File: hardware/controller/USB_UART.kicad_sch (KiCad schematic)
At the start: 0 parts

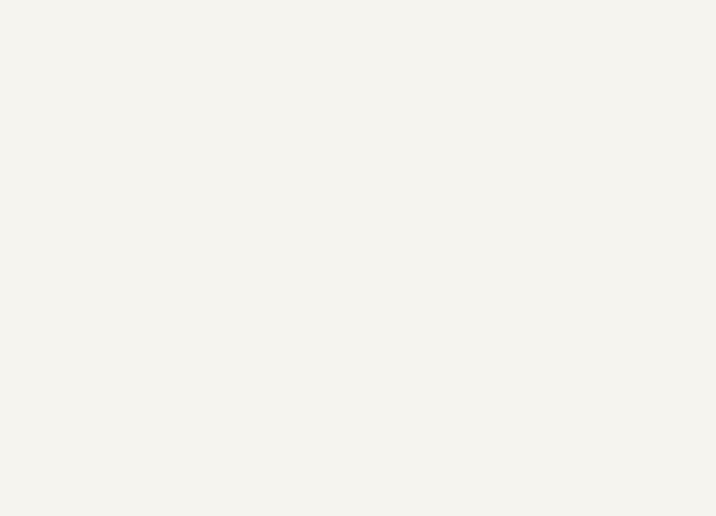
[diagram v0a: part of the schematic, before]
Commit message: added LED IC's and USB UART bridge
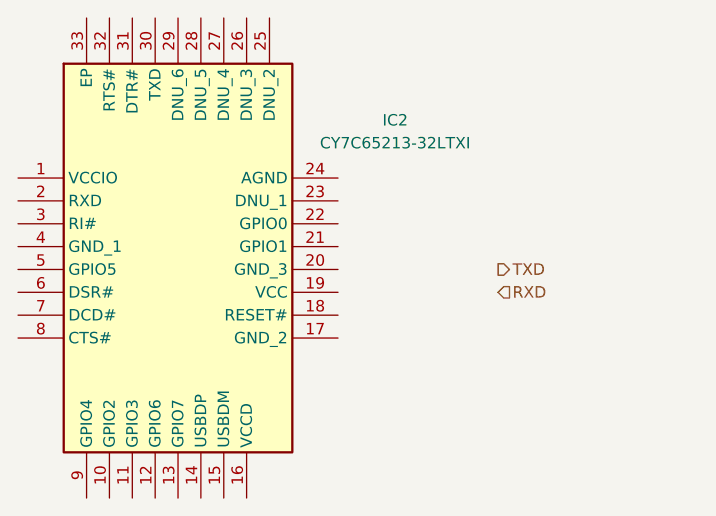
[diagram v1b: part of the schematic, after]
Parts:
- added IC2: CY7C65213-32LTXI, QFN50P500X500X100-33N-D, symbol SamacSys_Parts:CY7C65213-32LTXI
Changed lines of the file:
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@@
+		)
+	)
+	(hierarchical_label "RXD"
+		(shape input)
+		(at 148.59 83.82 0)
+		(effects
+			(font
+				(size 1.27 1.27)
+			)
+			(justify left)
 		)
 	)
@@
 		)
 	)
+	(hierarchical_label "TXD"
+		(shape output)
+		(at 148.59 81.28 0)
+		(effects
+			(font
+				(size 1.27 1.27)
+			)
+			(justify left)
+		)
+	)
+	(symbol
+		(lib_id "SamacSys_Parts:CY7C65213-32LTXI")
+		(at 95.25 71.12 0)
+		(unit 1)
+		(exclude_from_sim no)
+		(in_bom yes)
+		(on_board yes)
+		(dnp no)
+		(fields_autoplaced yes)
+		(property "Reference" "IC2"
+			(at 137.16 64.6998 0)
+			(effects
+				(font
+					(size 1.27 1.27)
+				)
+			)
+		)
+		(property "Value" "CY7C65213-32LTXI"
+			(at 137.16 67.2398 0)
+			(effects
+				(font
+					(size 1.27 1.27)
+				)
+			)
+		)
+		(property "Footprint" "QFN50P500X500X100-33N-D"
+			(at 127 155.88 0)
+			(effects
+				(font
+					(size 1.27 1.27)
+				)
+				(justify left top)
+				(hide yes)
+			)
+		)
+		(property "Datasheet" "https://www.cypress.com/file/139881/download"
+			(at 127 255.88 0)
+			(effects
+				(font
+					(size 1.27 1.27)
+				)
+				(justify left top)
+				(hide yes)
+			)
+		)
+		(property "Description" "USB Interface IC USB-UART LP Bridge Controller"
+			(at 95.25 71.12 0)
+			(effects
+				(font
+					(size 1.27 1.27)
+				)
+				(hide yes)
+			)
+		)
+		(property "Height" "1"
+			(at 127 455.88 0)
+			(effects
+				(font
+					(size 1.27 1.27)
+				)
+				(justify left top)
+				(hide yes)
+			)
+		)
+		(property "Mouser Part Number" "727-CY7C65213-32LTXI"
+			(at 127 555.88 0)
+			(effects
+				(font
+					(size 1.27 1.27)
+				)
+				(justify left top)
+				(hide yes)
+			)
+		)
+		(property "Mouser Price/Stock" "https://www.mouser.co.uk/ProductDetail/Cypress-Semiconductor/CY7C65213-32LTXI?qs=zaNmQhktveH29yVGSodaDg%3D%3D"
+			(at 127 655.88 0)
+			(effects
+				(font
+					(size 1.27 1.27)
+				)
+				(justify left top)
+				(hide yes)
+			)
+		)
+		(property "Manufacturer_Name" "Infineon"
+			(at 127 755.88 0)
+			(effects
+				(font
+					(size 1.27 1.27)
+				)
+				(justify left top)
+				(hide yes)
+			)
+		)
+		(property "Manufacturer_Part_Number" "CY7C65213-32LTXI"
+			(at 127 855.88 0)
+			(effects
+				(font
+					(size 1.27 1.27)
+				)
+				(justify left top)
+				(hide yes)
+			)
+		)
+		(pin "8"
+		)
+		(pin "3"
+		)
+		(pin "13"
+		)
+		(pin "25"
+		)
+		(pin "16"
+		)
+		(pin "6"
+		)
+		(pin "21"
+		)
+		(pin "19"
+		)
+		(pin "33"
+		)
+		(pin "5"
+		)
+		(pin "2"
+		)
+		(pin "9"
+		)
+		(pin "11"
+		)
+		(pin "30"
+		)
+		(pin "31"
+		)
+		(pin "12"
+		)
+		(pin "28"
+		)
+		(pin "27"
+		)
+		(pin "32"
+		)
+		(pin "4"
+		)
+		(pin "7"
+		)
+		(pin "29"
+		)
+		(pin "15"
+		)
+		(pin "1"
+		)
+		(pin "14"
+		)
+		(pin "10"
+		)
+		(pin "26"
+		)
+		(pin "24"
+		)
+		(pin "23"
+		)
+		(pin "22"
+		)
+		(pin "20"
+		)
+		(pin "17"
+		)
+		(pin "18"
+		)
+		(instances
+			(project ""
+				(path "/869bea87-c885-4ead-826b-3f34ceacafad/6716075d-3941-4cbb-90c0-6bb554220bff"
+					(reference "IC2")
+					(unit 1)
+				)
+			)
+		)
+	)

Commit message: asdasd
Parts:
- renumbered IC2 to IC1
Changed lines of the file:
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@@
 		(dnp no)
 		(fields_autoplaced yes)
-		(property "Reference" "IC2"
+		(property "Reference" "IC1"
 			(at 137.16 64.6998 0)
 			(effects
@@
 			(project ""
 				(path "/869bea87-c885-4ead-826b-3f34ceacafad/6716075d-3941-4cbb-90c0-6bb554220bff"
-					(reference "IC2")
+					(reference "IC1")
 					(unit 1)
 				)

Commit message: a
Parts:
- removed IC1: CY7C65213-32LTXI, QFN50P500X500X100-33N-D, symbol SamacSys_Parts:CY7C65213-32LTXI
- added C13: 4u3, symbol Device:C
- added C14: u1, symbol Device:C
- added IC3: CP2102N-A02-GQFN28, QFN50P500X500X80-29N-D, symbol SamacSys_Parts:CP2102N-A02-GQFN28
- added R27: 22k5, symbol Device:R
- added R28: 47k5, symbol Device:R
- added R29: 2k, symbol Device:R
- added R30: 10k, symbol Device:R
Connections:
- net RXD: now also IC3.25 (RXD)
- net TXD: now also IC3.26 (TXD)
- new net: IC3.11 (SUSPENDB), R30.2
- new net: IC3.8 (VBUS), R27.2, R28.2
- new net: IC3.9 (RSTB), R29.1
- new net +3V3: C13.1, C14.1, IC3.6 (VDD), IC3.7 (VREGIN), R29.2
- new net DTR: IC3.28 (DTR)
- new net GND: C13.2, C14.2, IC3.29 (BGND), IC3.3 (GND), R28.1, R30.1
- new net RTS: IC3.24 (RTS)
- new net USB+: IC3.4 (D+)
- new net USB-: IC3.5 (D-)
- new net VBUS: R27.1
- no-connect marks 0 -> 15

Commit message: fixed bus stuff
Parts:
- renumbered C13 to C12, C14 to C13, IC3 to IC1, R29 to R11, R27 to R12, R28 to R13, R30 to R14
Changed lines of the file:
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@@
 		(on_board yes)
 		(dnp no)
-		(property "Reference" "R30"
+		(property "Reference" "R14"
 			(at 118.11 130.81 0)
 			(effects
@@
 			(project "controller"
 				(path "/869bea87-c885-4ead-826b-3f34ceacafad/6716075d-3941-4cbb-90c0-6bb554220bff"
-					(reference "R30")
+					(reference "R14")
 					(unit 1)
 				)
@@
 		(on_board yes)
 		(dnp no)
-		(property "Reference" "IC3"
+		(property "Reference" "IC1"
 			(at 125.984 65.786 0)
 			(effects
@@
 			(project ""
 				(path "/869bea87-c885-4ead-826b-3f34ceacafad/6716075d-3941-4cbb-90c0-6bb554220bff"
-					(reference "IC3")
+					(reference "IC1")
 					(unit 1)
 				)
@@
 		(dnp no)
 		(fields_autoplaced yes)
-		(property "Reference" "C14"
+		(property "Reference" "C13"
 			(at 96.52 107.9499 0)
 			(effects
@@
 			(project "controller"
 				(path "/869bea87-c885-4ead-826b-3f34ceacafad/6716075d-3941-4cbb-90c0-6bb554220bff"
-					(reference "C14")
+					(reference "C13")
 					(unit 1)
 				)
@@
 		(on_board yes)
 		(dnp no)
-		(property "Reference" "#PWR045"
+		(property "Reference" "#PWR035"
 			(at 86.36 107.95 0)
 			(effects
@@
 			(project ""
 				(path "/869bea87-c885-4ead-826b-3f34ceacafad/6716075d-3941-4cbb-90c0-6bb554220bff"
-					(reference "#PWR045")
+					(reference "#PWR035")
 					(unit 1)
 				)
@@
 		(on_board yes)
 		(dnp no)
-		(property "Reference" "R27"
+		(property "Reference" "R12"
 			(at 93.98 122.428 90)
 			(effects
@@
 			(project ""
 				(path "/869bea87-c885-4ead-826b-3f34ceacafad/6716075d-3941-4cbb-90c0-6bb554220bff"
-					(reference "R27")
+					(reference "R12")
 					(unit 1)
 				)
@@
 		(dnp no)
 		(fields_autoplaced yes)
-		(property "Reference" "#PWR048"
+		(property "Reference" "#PWR038"
 			(at 124.46 142.24 0)
 			(effects
@@
 			(project "controller"
 				(path "/869bea87-c885-4ead-826b-3f34ceacafad/6716075d-3941-4cbb-90c0-6bb554220bff"
-					(reference "#PWR048")
+					(reference "#PWR038")
 					(unit 1)
 				)
@@
 		(dnp no)
 		(fields_autoplaced yes)
-		(property "Reference" "#PWR046"
+		(property "Reference" "#PWR036"
 			(at 87.63 121.92 0)
 			(effects
@@
 			(project ""
 				(path "/869bea87-c885-4ead-826b-3f34ceacafad/6716075d-3941-4cbb-90c0-6bb554220bff"
-					(reference "#PWR046")
+					(reference "#PWR036")
 					(unit 1)
 				)
@@
 		(dnp no)
 		(fields_autoplaced yes)
-		(property "Reference" "R28"
+		(property "Reference" "R13"
 			(at 101.6 130.8099 0)
 			(effects
@@
 			(project "controller"
 				(path "/869bea87-c885-4ead-826b-3f34ceacafad/6716075d-3941-4cbb-90c0-6bb554220bff"
-					(reference "R28")
+					(reference "R13")
 					(unit 1)
 				)
@@
 		(on_board yes)
 		(dnp no)
-		(property "Reference" "#PWR036"
+		(property "Reference" "#PWR034"
 			(at 85.09 85.09 0)
 			(effects
@@
 			(project "controller"
 				(path "/869bea87-c885-4ead-826b-3f34ceacafad/6716075d-3941-4cbb-90c0-6bb554220bff"
-					(reference "#PWR036")
+					(reference "#PWR034")
 					(unit 1)
 				)
@@
 		(dnp no)
 		(fields_autoplaced yes)
-		(property "Reference" "C13"
+		(property "Reference" "C12"
 			(at 85.09 107.9499 0)
 			(effects
@@
 			(project ""
 				(path "/869bea87-c885-4ead-826b-3f34ceacafad/6716075d-3941-4cbb-90c0-6bb554220bff"
-					(reference "C13")
+					(reference "C12")
 					(unit 1)
 				)
@@
 		(dnp no)
 		(fields_autoplaced yes)
-		(property "Reference" "#PWR037"
+		(property "Reference" "#PWR039"
 			(at 133.35 142.24 0)
 			(effects
@@
 			(project "controller"
 				(path "/869bea87-c885-4ead-826b-3f34ceacafad/6716075d-3941-4cbb-90c0-6bb554220bff"
-					(reference "#PWR037")
+					(reference "#PWR039")
 					(unit 1)
 				)
@@
 		(on_board yes)
 		(dnp no)
-		(property "Reference" "R29"
+		(property "Reference" "R11"
 			(at 86.36 83.82 0)
 			(effects
@@
 			(project "controller"
 				(path "/869bea87-c885-4ead-826b-3f34ceacafad/6716075d-3941-4cbb-90c0-6bb554220bff"
-					(reference "R29")
+					(reference "R11")
 					(unit 1)
 				)
@@
 		(dnp no)
 		(fields_autoplaced yes)
-		(property "Reference" "#PWR047"
+		(property "Reference" "#PWR037"
 			(at 99.06 142.24 0)
 			(effects
@@
 			(project "controller"
 				(path "/869bea87-c885-4ead-826b-3f34ceacafad/6716075d-3941-4cbb-90c0-6bb554220bff"
-					(reference "#PWR047")
-					(unit 1)
-				)
+					(reference "#PWR037")
+					(unit 1)
+				)

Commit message: modified power circuitry
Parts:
- IC1: footprint QFN50P500X500X80-29N-D -> SamacSys_Parts:QFN50P500X500X80-29N-D
- R11: value 2k -> 1k
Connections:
- net DTR renamed UART.DTR
- net RTS renamed UART.RTS
- net RXD renamed UART.RXD
- net TXD renamed UART.TXD
- net VBUS renamed USBC_VBUS

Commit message: finished first rev of controller schematic minus actually finding passive components. moved some features to rev2 todo
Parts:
- R12: value 22k5 -> 22k1
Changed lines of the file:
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@@
 			)
 		)
-		(property "Value" "22k5"
+		(property "Value" "22k1"
 			(at 93.98 124.968 90)
 			(effects

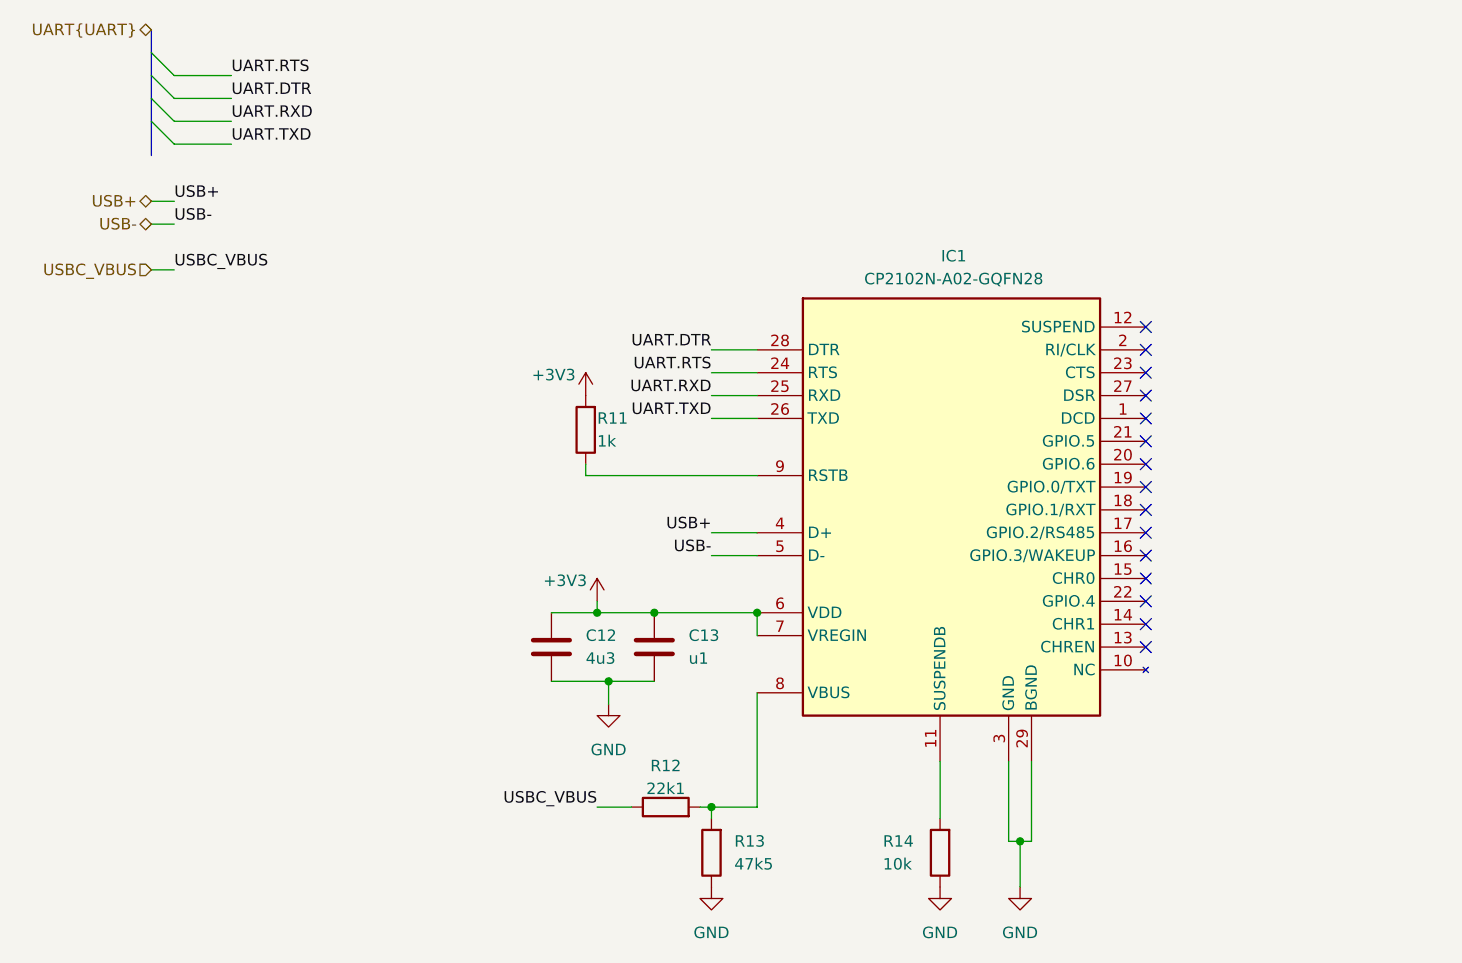
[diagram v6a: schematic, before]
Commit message: Moved LEDs around. Replaced some discrete resistors with resistor arrays. Added mounting holes. Added. Added a lot of actual components for passive elements
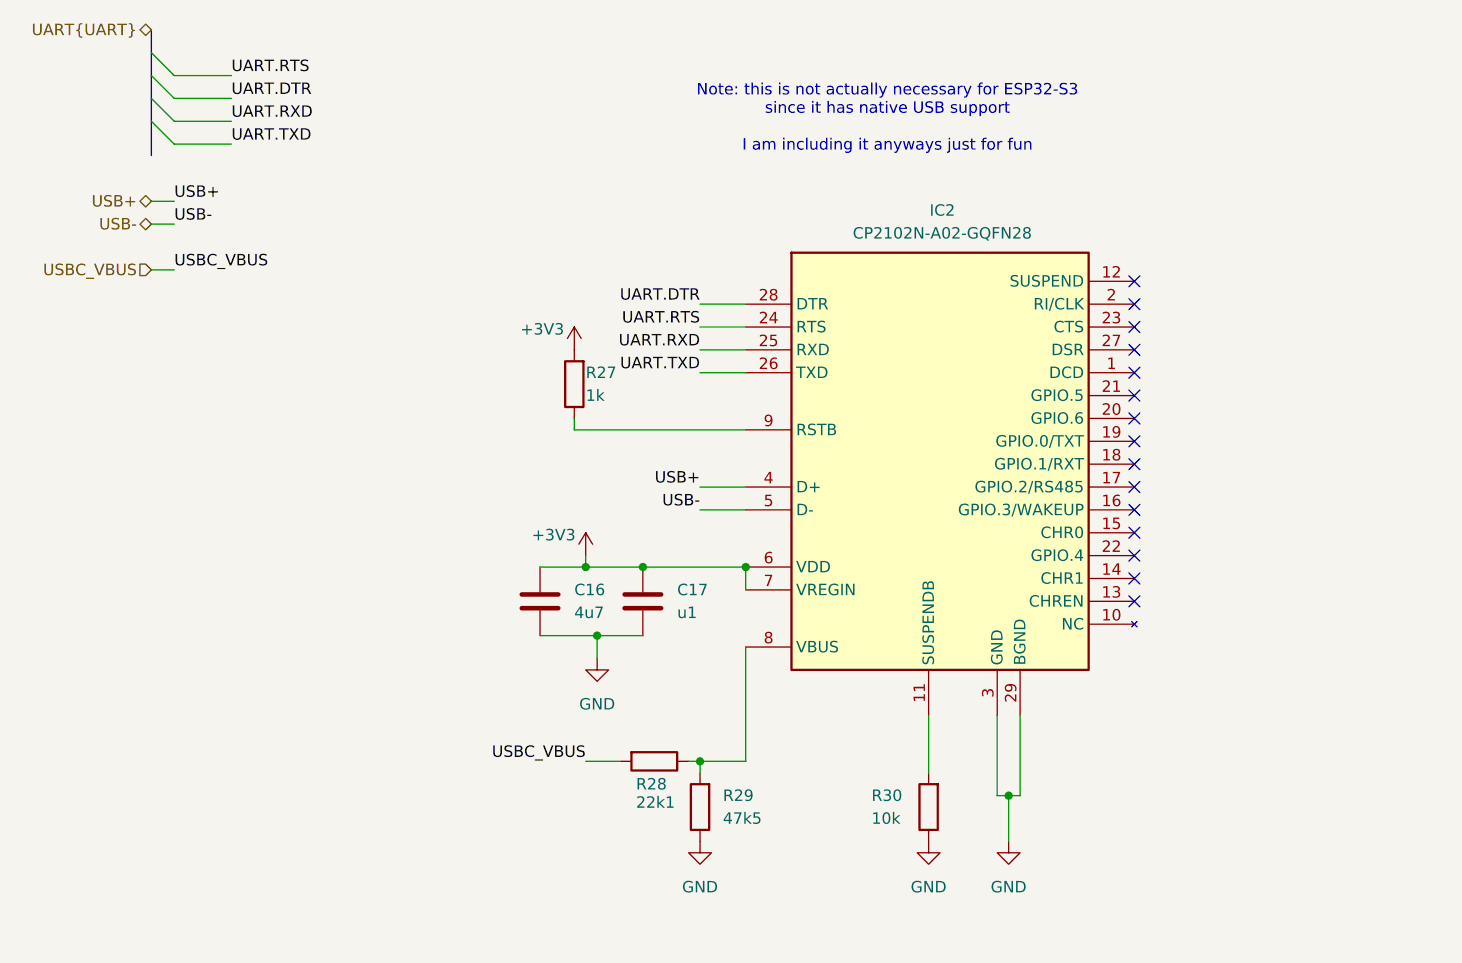
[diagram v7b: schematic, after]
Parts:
- C16: renamed from C12; value 4u3 -> 4u7
- C17: renamed from C13; footprint (none) -> MAJx16; Manufacturer_Name (none) -> TAIYO YUDEN; Manufacturer_Part_Number (none) -> MAJCH168BB7104KTEA01; Mouser Part Number (none) -> 963-MAJCH168BB7104KT; Mouser Price/Stock (none) -> https://www.mouser.co.uk/ProductDetail/TAIYO-YUDEN/MAJCH168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
- IC2: renamed from IC1; footprint SamacSys_Parts:QFN50P500X500X80-29N-D -> QFN50P500X500X80-29N-D
- R27: renamed from R11; footprint (none) -> RESC3116X65N; Height (none) -> 0.65; Manufacturer_Name (none) -> YAGEO; Manufacturer_Part_Number (none) -> RC1206FR-131KL; Mouser Part Number (none) -> 603-RC1206FR-131KL; Mouser Price/Stock (none) -> https://www.mouser.co.uk/ProductDetail/YAGEO/RC1206FR-131KL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
- R28: renamed from R12; footprint (none) -> Resistor_SMD:R_0603_1608Metric; Manufacturer_Name (none) -> Vishay; Manufacturer_Part_Number (none) -> CRCW060322K1FKEBC; Mouser Part Number (none) -> 71-CRCW060322K1FKEBC; Mouser Price/Stock (none) -> https://www.mouser.com/ProductDetail/Vishay/CRCW060322K1FKE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
- R30: renamed from R14; footprint (none) -> RESC2012X60N; Height (none) -> 0.6; Manufacturer_Name (none) -> TT Electronics; Manufacturer_Part_Number (none) -> ASC0805-10KFT5; Mouser Part Number (none) -> 756-ASC0805-10KFT5; Mouser Price/Stock (none) -> https://www.mouser.co.uk/ProductDetail/Welwyn-Components-TT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
- renumbered R13 to R29
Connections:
- net USBC_VBUS: now also R28.2; no longer R28.1
- net at IC2.8 (VBUS), R29.2: now also R28.1; no longer R28.2
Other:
- note added: "Note: this is not actually necessary for ESP32-S3 since it has native USB support I am including it anyways just for fun"
- moved on the sheet: C16, C17, IC2, R27, R28, R29, R30

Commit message: ERC good to go. grouped all components on pcb
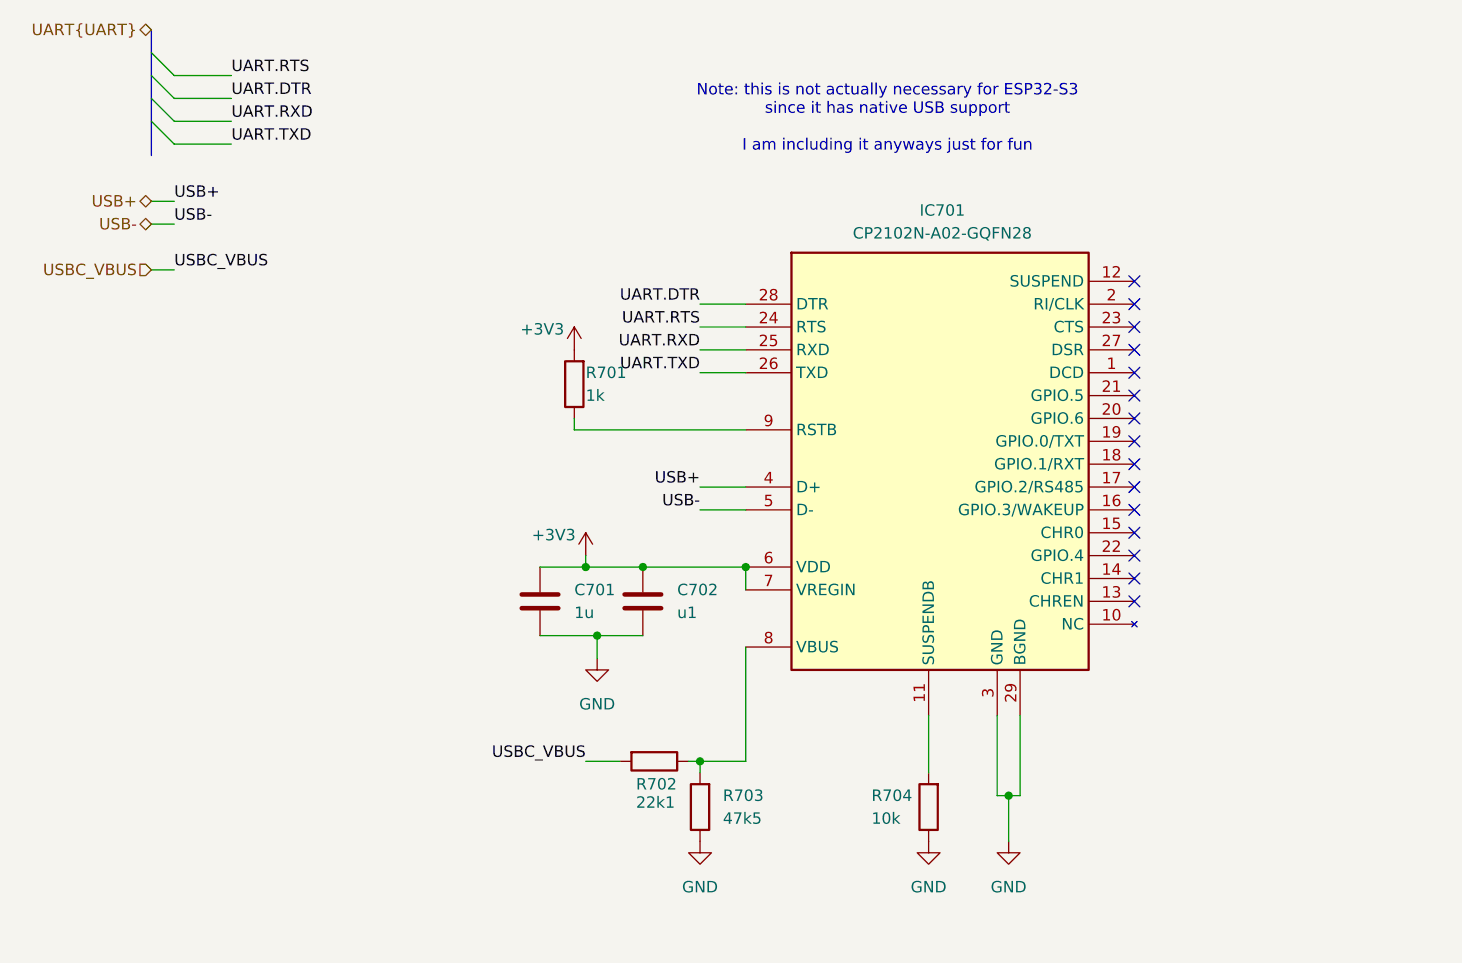
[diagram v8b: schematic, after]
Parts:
- removed C16: 4u7, symbol Device:C
- added C701: 1u, SamacSys_Parts:CAPC2012X135N, symbol Device:C
- C702: renamed from C17; footprint MAJx16 -> SamacSys_Parts:MAJx16
- IC701: renamed from IC2; footprint QFN50P500X500X80-29N-D -> SamacSys_Parts:QFN50P500X500X80-29N-D
- R701: renamed from R27; footprint RESC3116X65N -> SamacSys_Parts:RESC3116X65N
- R703: renamed from R29; footprint (none) -> SamacSys_Parts:RESC1608X55N; Height (none) -> 0.55; Manufacturer_Name (none) -> Bourns; Manufacturer_Part_Number (none) -> CR0603-FX-4752ELF; Mouser Part Number (none) -> 652-CR0603FX-4752ELF; Mouser Price/Stock (none) -> https://www.mouser.co.uk/ProductDetail/Bourns/CR0603-FX-475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
- R704: renamed from R30; footprint RESC2012X60N -> SamacSys_Parts:RESC2012X60N
- renumbered R28 to R702
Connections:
- net +3V3: now also C701.1
- net GND: now also C701.2
